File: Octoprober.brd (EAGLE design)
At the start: 130.8 x 86.9 mm, 111 parts, among them J1 10118193-0001LF, J2 26-60-4020, P1 TC33X-1, SW1 101-0134-EV, SW2 EVQ-Q2203W, SW3 EVQ-Q2203W, SW4 EVQ-Q2203W, SW5 EVQ-Q2203W, U1 P8X32A-M44, U10 MAX31855KASA+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

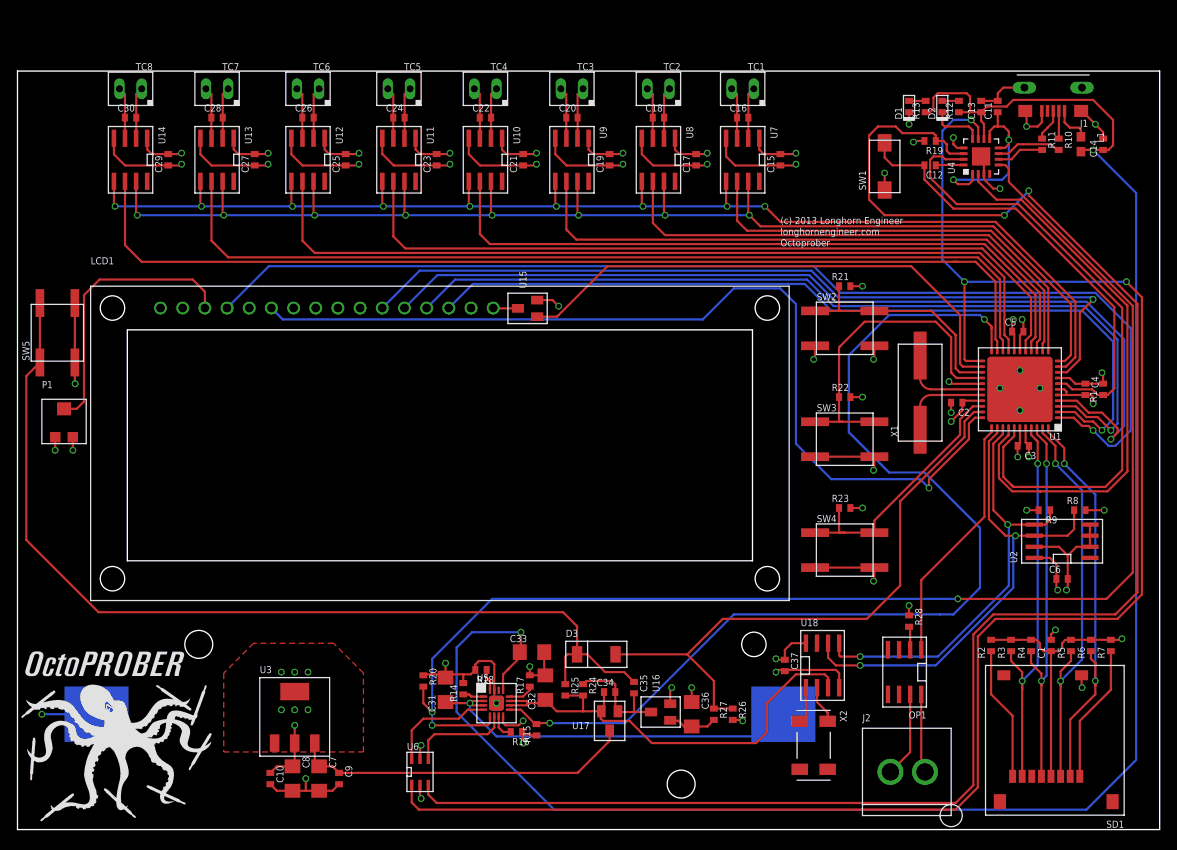
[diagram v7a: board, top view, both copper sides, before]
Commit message: Added TVS to TC lines.
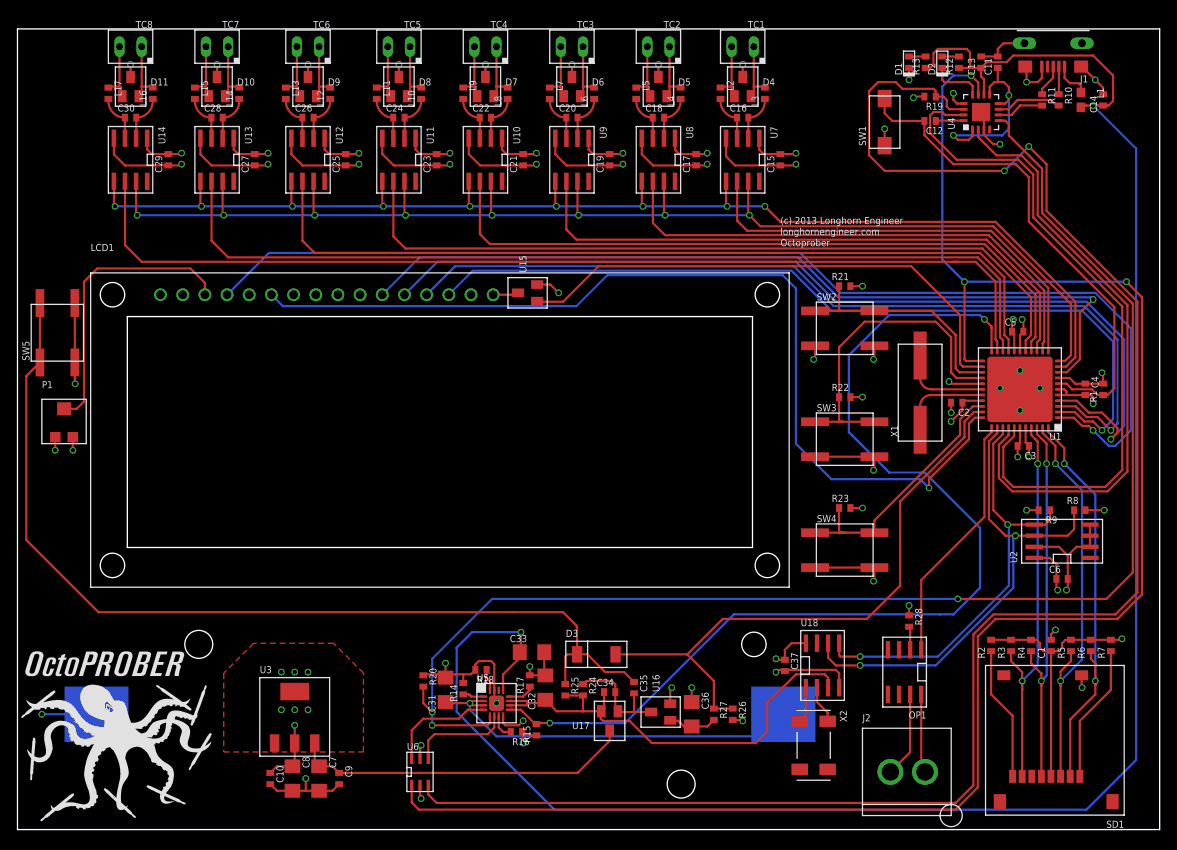
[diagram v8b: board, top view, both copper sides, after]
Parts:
- added D10, D11, D4, D5, D6, D7, D8, D9: NUP2105LT1G, PP_Passives:SOT-23
- added L10, L11, L12, L13, L14, L15, L16, L17, L2, L3, L4, L5, L6, L7, L8, L9: BK1005HM471-T, PP_Passives:0402
- L1: device PP_Passives:0603 -> PP_Passives:0603@1
- moved C12 5.08 mm to (104.5, 81.2)
- moved C11 5.08 mm to (112.3, 87.9)
- moved C13 5.08 mm to (110.4, 87.9)
- moved C14 5.08 mm to (124.3, 83.6)
- moved D1 5.08 mm to (102.1, 87.9)
- moved D2 5.08 mm to (105.9, 87.9)
- moved J1 5.08 mm to (118.6, 89.9)
- moved L1 5.08 mm to (121.8, 83.6)
- moved R10 5.08 mm to (119.3, 83.6)
- moved R11 5.08 mm to (117.3, 83.6)
- moved R12 5.08 mm to (107.8, 87.9)
- moved R13 5.08 mm to (104.0, 87.9)
- moved R19 5.08 mm to (104.5, 83.9)
- moved SW1 5.08 mm to (99.3, 81.0)
- moved U4 5.08 mm to (110.4, 82.2)
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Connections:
- new net N$10: D6.1, L7.1, TC3.2
- new net N$11: D6.2, L6.2, TC3.1
- new net N$12: D7.1, L9.1, TC4.2
- new net N$13: D7.2, L8.2, TC4.1
- new net N$14: D11.1, L17.1, TC8.2
- new net N$15: D11.2, L16.2, TC8.1
- new net N$16: D10.1, L15.1, TC7.2
- new net N$17: D10.2, L14.2, TC7.1
- new net N$18: D9.1, L13.1, TC6.2
- new net N$19: D9.2, L12.2, TC6.1
- new net N$2: D4.1, L2.1, TC1.2
- new net N$20: D8.1, L11.1, TC5.2
- new net N$21: D8.2, L10.2, TC5.1
- new net N$7: D4.2, L3.2, TC1.1
- new net N$8: D5.1, L5.1, TC2.2
- new net N$9: D5.2, L4.2, TC2.1
- net GND: now also D10.3, D11.3, D4.3, D5.3, D6.3, D7.3, D8.3, D9.3
- net TP_T+_0: now also L2.2; no longer TC1.2
- net TP_T+_1: now also L5.2; no longer TC2.2
- net TP_T+_2: now also L7.2; no longer TC3.2
- net TP_T+_3: now also L9.2; no longer TC4.2
- net TP_T+_4: now also L11.2; no longer TC5.2
- net TP_T+_5: now also L13.2; no longer TC6.2
- net TP_T+_6: now also L15.2; no longer TC7.2
- net TP_T+_7: now also L17.2; no longer TC8.2
- net TP_T-_0: now also L3.1; no longer TC1.1
- net TP_T-_1: now also L4.1; no longer TC2.1
- net TP_T-_2: now also L6.1; no longer TC3.1
- net TP_T-_3: now also L8.1; no longer TC4.1
- net TP_T-_4: now also L10.1; no longer TC5.1
- net TP_T-_5: now also L12.1; no longer TC6.1
- net TP_T-_6: now also L14.1; no longer TC7.1
- net TP_T-_7: now also L16.1; no longer TC8.1
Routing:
- net GND: track 282.8 -> 376.6 mm, vias 49 -> 57
- net N$7: track 0.00 -> 7.57 mm
- net N$9: track 0.00 -> 7.37 mm
- net N$8: track 0.00 -> 7.37 mm
- net N$21: track 0.00 -> 7.37 mm
- net N$19: track 0.00 -> 7.37 mm
- net N$13: track 0.00 -> 7.37 mm
- net N$11: track 0.00 -> 7.37 mm
- net N$17: track 0.00 -> 7.37 mm
- net N$16: track 0.00 -> 7.37 mm
- net N$15: track 0.00 -> 7.37 mm
- net N$14: track 0.00 -> 7.37 mm
- net N$20: track 0.00 -> 7.37 mm
- net N$18: track 0.00 -> 7.37 mm
- net N$12: track 0.00 -> 7.37 mm
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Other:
- board size 130.8 x 86.9 mm -> 130.8 x 91.7 mm
